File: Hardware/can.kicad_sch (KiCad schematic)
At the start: 9 parts, among them U20 SN65HVD230

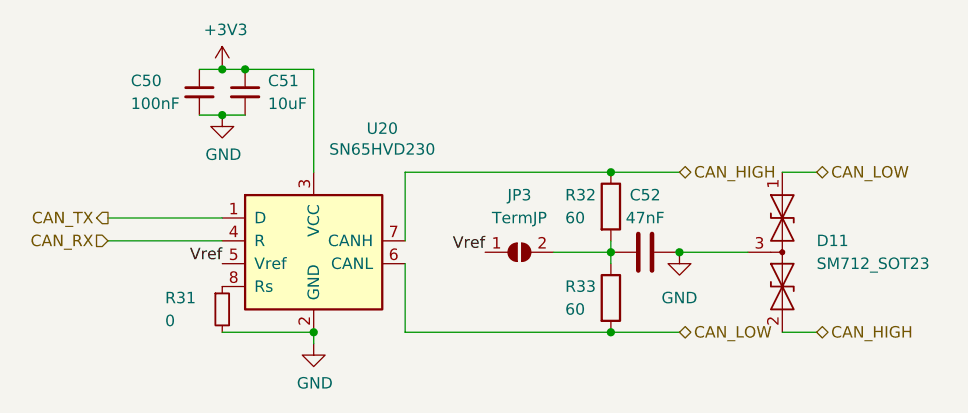
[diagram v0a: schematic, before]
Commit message: cleaned up schematic and bom
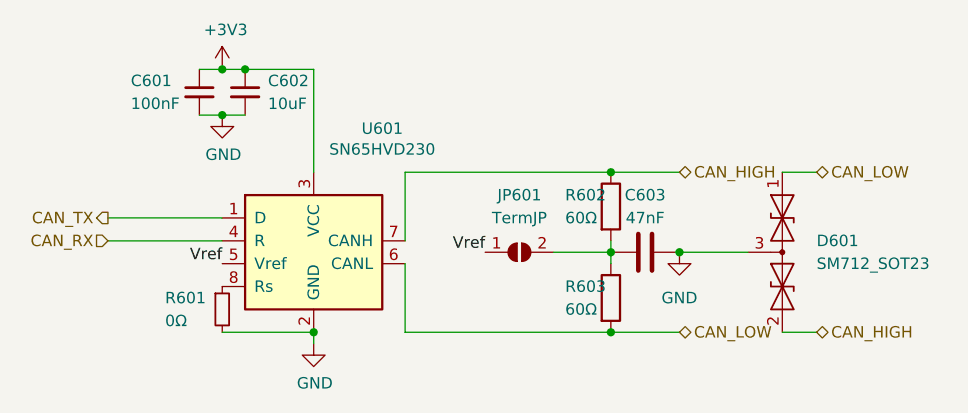
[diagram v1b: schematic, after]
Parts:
- JP601: renamed from JP3; now left out of the parts list
- R601: renamed from R31; value 0 -> 0Ω
- R602: renamed from R32; value 60 -> 60Ω
- R603: renamed from R33; value 60 -> 60Ω
- renumbered C50 to C601, C51 to C602, C52 to C603, D11 to D601, U20 to U601
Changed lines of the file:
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@@
 (kicad_sch
-	(version 20231120)
+	(version 20250114)
 	(generator "eeschema")
-	(generator_version "8.0")
+	(generator_version "9.0")
 	(paper "A4")
 	(junction
@@
 		(dnp no)
 		(fields_autoplaced yes)
-		(property "Reference" "#PWR0123"
+		(property "Reference" "#PWR0603"
 			(at 134.62 105.41 0)
 			(effects
@@
 			(project "PickleRick"
 				(path "/e63e39d7-6ac0-4ffd-8aa3-1841a4541b55/84dc3251-c581-43e1-8e86-e53b5efc8269"
-					(reference "#PWR0123")
+					(reference "#PWR0603")
 					(unit 1)
 				)
@@
 		(dnp no)
 		(fields_autoplaced yes)
-		(property "Reference" "#PWR0121"
+		(property "Reference" "#PWR0601"
 			(at 124.46 72.39 0)
 			(effects
@@
 			(project "PickleRick"
 				(path "/e63e39d7-6ac0-4ffd-8aa3-1841a4541b55/84dc3251-c581-43e1-8e86-e53b5efc8269"
-					(reference "#PWR0121")
+					(reference "#PWR0601")
 					(unit 1)
 				)
@@
 		(dnp no)
 		(fields_autoplaced yes)
-		(property "Reference" "U20"
+		(property "Reference" "U601"
 			(at 142.24 75.1586 0)
 			(effects
@@
 			(project "PickleRick"
 				(path "/e63e39d7-6ac0-4ffd-8aa3-1841a4541b55/84dc3251-c581-43e1-8e86-e53b5efc8269"
-					(reference "U20")
+					(reference "U601")
 					(unit 1)
 				)
@@
 		(dnp no)
 		(fields_autoplaced yes)
-		(property "Reference" "C51"
+		(property "Reference" "C602"
 			(at 129.54 69.8562 0)
 			(effects
@@
 			(project "PickleRick"
 				(path "/e63e39d7-6ac0-4ffd-8aa3-1841a4541b55/84dc3251-c581-43e1-8e86-e53b5efc8269"
-					(reference "C51")
+					(reference "C602")
 					(unit 1)
 				)
@@
 		(dnp no)
 		(fields_autoplaced yes)
-		(property "Reference" "D11"
+		(property "Reference" "D601"
 			(at 190.5 87.63 90)
 			(effects
@@
 			(project "PickleRick"
 				(path "/e63e39d7-6ac0-4ffd-8aa3-1841a4541b55/84dc3251-c581-43e1-8e86-e53b5efc8269"
-					(reference "D11")
+					(reference "D601")
 					(unit 1)
 				)
@@
 		(dnp no)
 		(fields_autoplaced yes)
-		(property "Reference" "#PWR0124"
+		(property "Reference" "#PWR0604"
 			(at 175.26 95.25 0)
 			(effects
@@
 			(project "PickleRick"
 				(path "/e63e39d7-6ac0-4ffd-8aa3-1841a4541b55/84dc3251-c581-43e1-8e86-e53b5efc8269"
-					(reference "#PWR0124")
+					(reference "#PWR0604")
 					(unit 1)
 				)
@@
 		(dnp no)
 		(fields_autoplaced yes)
-		(property "Reference" "C50"
+		(property "Reference" "C601"
 			(at 114.3 69.85 0)
 			(effects
@@
 			(project "PickleRick"
 				(path "/e63e39d7-6ac0-4ffd-8aa3-1841a4541b55/84dc3251-c581-43e1-8e86-e53b5efc8269"
-					(reference "C50")
+					(reference "C601")
 					(unit 1)
 				)
@@
 		(on_board yes)
 		(dnp no)
-		(property "Reference" "R31"
+		(property "Reference" "R601"
 			(at 118.11 93.98 0)
 			(effects
@@
 			)
 		)
-		(property "Value" "0"
+		(property "Value" "0Ω"
 			(at 118.11 96.52 0)
 			(effects
@@
 			(project "PickleRick"
 				(path "/e63e39d7-6ac0-4ffd-8aa3-1841a4541b55/84dc3251-c581-43e1-8e86-e53b5efc8269"
-					(reference "R31")
+					(reference "R601")
 					(unit 1)
 				)
@@
 		(dnp no)
 		(fields_autoplaced yes)
-		(property "Reference" "R33"
+		(property "Reference" "R603"
 			(at 162.56 92.71 0)
 			(effects
@@
 			)
 		)
-		(property "Value" "60"
+		(property "Value" "60Ω"
 			(at 162.56 95.25 0)
 			(effects
@@
 			(project "PickleRick"
 				(path "/e63e39d7-6ac0-4ffd-8aa3-1841a4541b55/84dc3251-c581-43e1-8e86-e53b5efc8269"
-					(reference "R33")
+					(reference "R603")
 					(unit 1)
 				)
@@
 		(dnp no)
 		(fields_autoplaced yes)
-		(property "Reference" "R32"
+		(property "Reference" "R602"
 			(at 162.56 82.55 0)
 			(effects
@@
 			)
 		)
-		(property "Value" "60"
+		(property "Value" "60Ω"
 			(at 162.56 85.09 0)
 			(effects
@@
 			(project "PickleRick"
 				(path "/e63e39d7-6ac0-4ffd-8aa3-1841a4541b55/84dc3251-c581-43e1-8e86-e53b5efc8269"
-					(reference "R32")
+					(reference "R602")
 					(unit 1)
 				)
@@
 		(dnp no)
 		(fields_autoplaced yes)
-		(property "Reference" "C52"
+		(property "Reference" "C603"
 			(at 171.45 82.55 90)
 			(effects
@@
 			(project "PickleRick"
 				(path "/e63e39d7-6ac0-4ffd-8aa3-1841a4541b55/84dc3251-c581-43e1-8e86-e53b5efc8269"
-					(reference "C52")
+					(reference "C603")
 					(unit 1)
 				)
@@
 		(dnp no)
 		(fields_autoplaced yes)
-		(property "Reference" "#PWR0122"
+		(property "Reference" "#PWR0602"
 			(at 124.46 80.01 0)
 			(effects
@@
 			(project "PickleRick"
 				(path "/e63e39d7-6ac0-4ffd-8aa3-1841a4541b55/84dc3251-c581-43e1-8e86-e53b5efc8269"
-					(reference "#PWR0122")
+					(reference "#PWR0602")
 					(unit 1)
 				)
@@
 		(unit 1)
 		(exclude_from_sim no)
-		(in_bom yes)
+		(in_bom no)
 		(on_board yes)
 		(dnp no)
 		(fields_autoplaced yes)
-		(property "Reference" "JP3"
+		(property "Reference" "JP601"
 			(at 157.48 82.55 0)
 			(effects
@@
 			(project "PickleRick"
 				(path "/e63e39d7-6ac0-4ffd-8aa3-1841a4541b55/84dc3251-c581-43e1-8e86-e53b5efc8269"
-					(reference "JP3")
-					(unit 1)
-				)
+					(reference "JP601")
+					(unit 1)
+				)
